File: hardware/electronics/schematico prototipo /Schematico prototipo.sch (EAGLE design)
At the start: 6 parts, among them IC1 7404N

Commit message: modifiche schematico prototipo
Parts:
- added U$6: REGOLATORE-3.3V-1A, libreria valerio:REGOLATORE-3.3V-1A
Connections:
- new net 12V: U$6.VIN
- net 3.3V: now also U$6.VOUT
- net GND: now also U$6.GND
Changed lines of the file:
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@@
 <part name="U$5" library="VHN5019" deviceset="VHN5019" device=""/>
 <part name="IC1" library="74xx-eu" library_urn="urn:adsk.eagle:library:85" deviceset="74*04" device="N" package3d_urn="urn:adsk.eagle:package:2008/1"/>
+<part name="U$6" library="libreria valerio" deviceset="REGOLATORE-3.3V-1A" device=""/>
 </parts>
 <sheets>
@@
 <instance part="IC1" gate="C" x="160.02" y="170.18"/>
 <instance part="IC1" gate="D" x="5.08" y="167.64"/>
+<instance part="U$6" gate="G$1" x="180.34" y="121.92"/>
 </instances>
 <busses>
@@
 <label x="17.78" y="76.2" size="1.27" layer="95" rot="R180" xref="yes"/>
 </segment>
+<segment>
+<pinref part="U$6" gate="G$1" pin="GND"/>
+<wire x1="180.34" y1="109.22" x2="180.34" y2="106.68" width="0.1524" layer="91"/>
+<label x="180.34" y="106.68" size="1.778" layer="95" rot="R270" xref="yes"/>
+</segment>
 </net>
 <net name="3.3V" class="0">
@@
 <label x="132.08" y="139.7" size="1.27" layer="95" xref="yes"/>
 </segment>
+<segment>
+<pinref part="U$6" gate="G$1" pin="VOUT"/>
+<wire x1="195.58" y1="119.38" x2="200.66" y2="119.38" width="0.1524" layer="91"/>
+<label x="200.66" y="119.38" size="1.778" layer="95" xref="yes"/>
+</segment>
 </net>
+<net name="12V" class="0">
+<segment>
+<pinref part="U$6" gate="G$1" pin="VIN"/>
+<wire x1="167.64" y1="119.38" x2="162.56" y2="119.38" width="0.1524" layer="91"/>
+<label x="162.56" y="119.38" size="1.778" layer="95" rot="R180" xref="yes"/>
+</segment>
+</net>

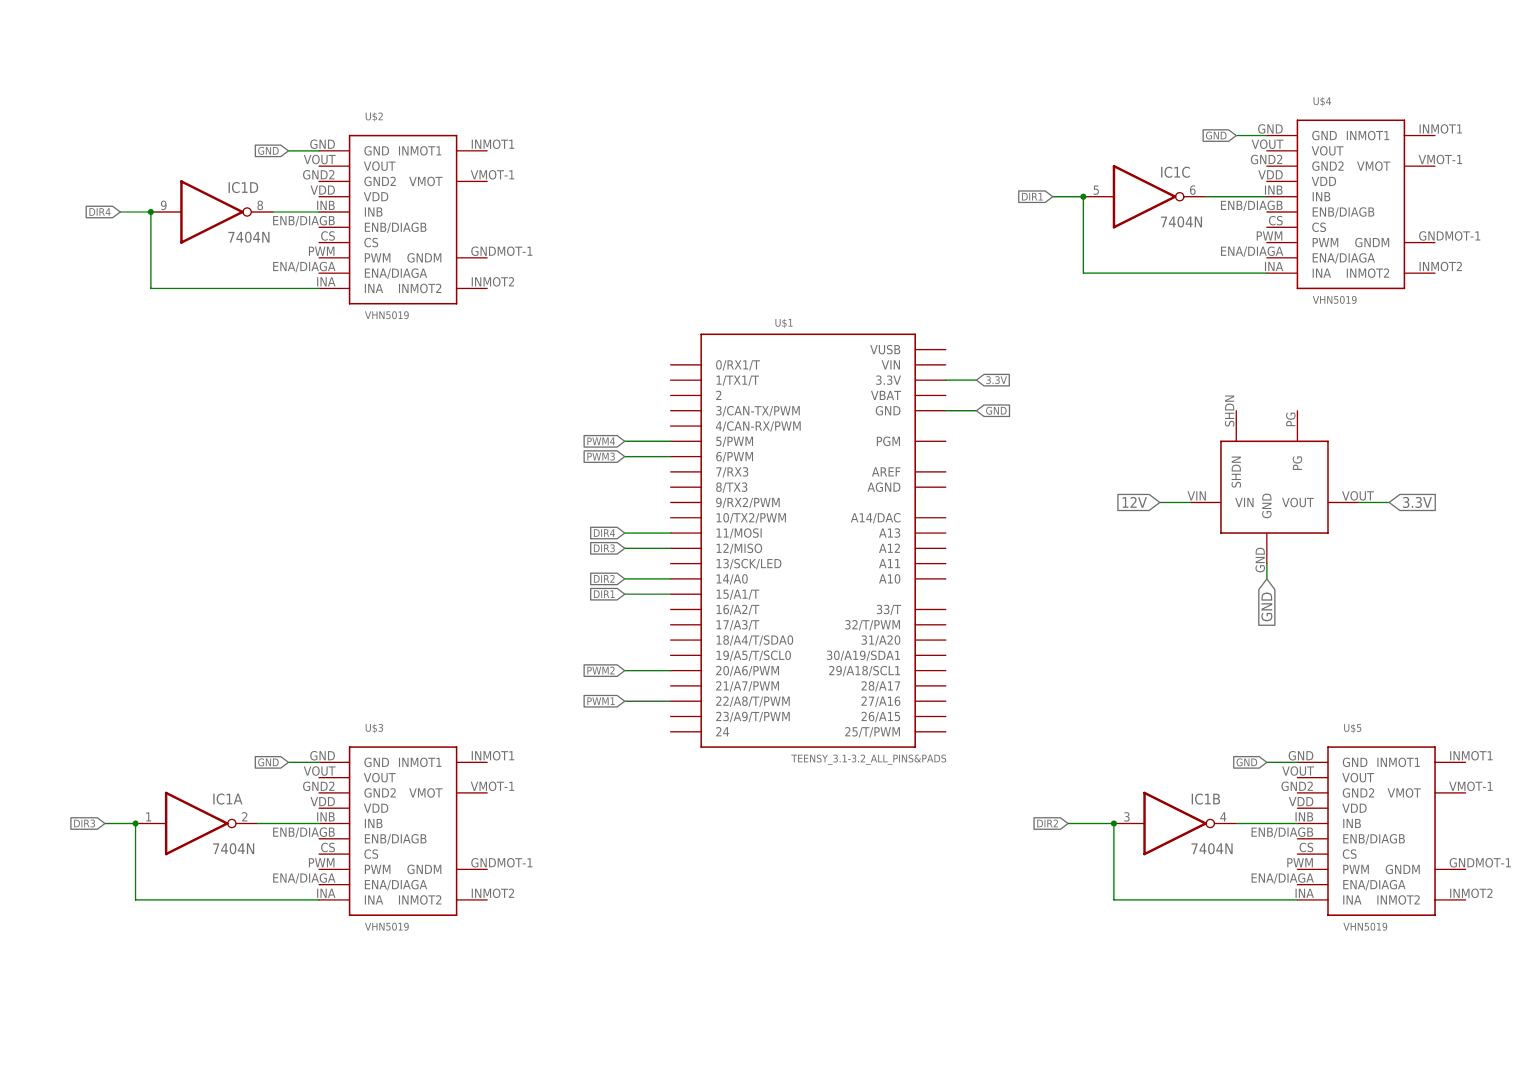
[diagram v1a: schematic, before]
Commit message: aggiunta step-down
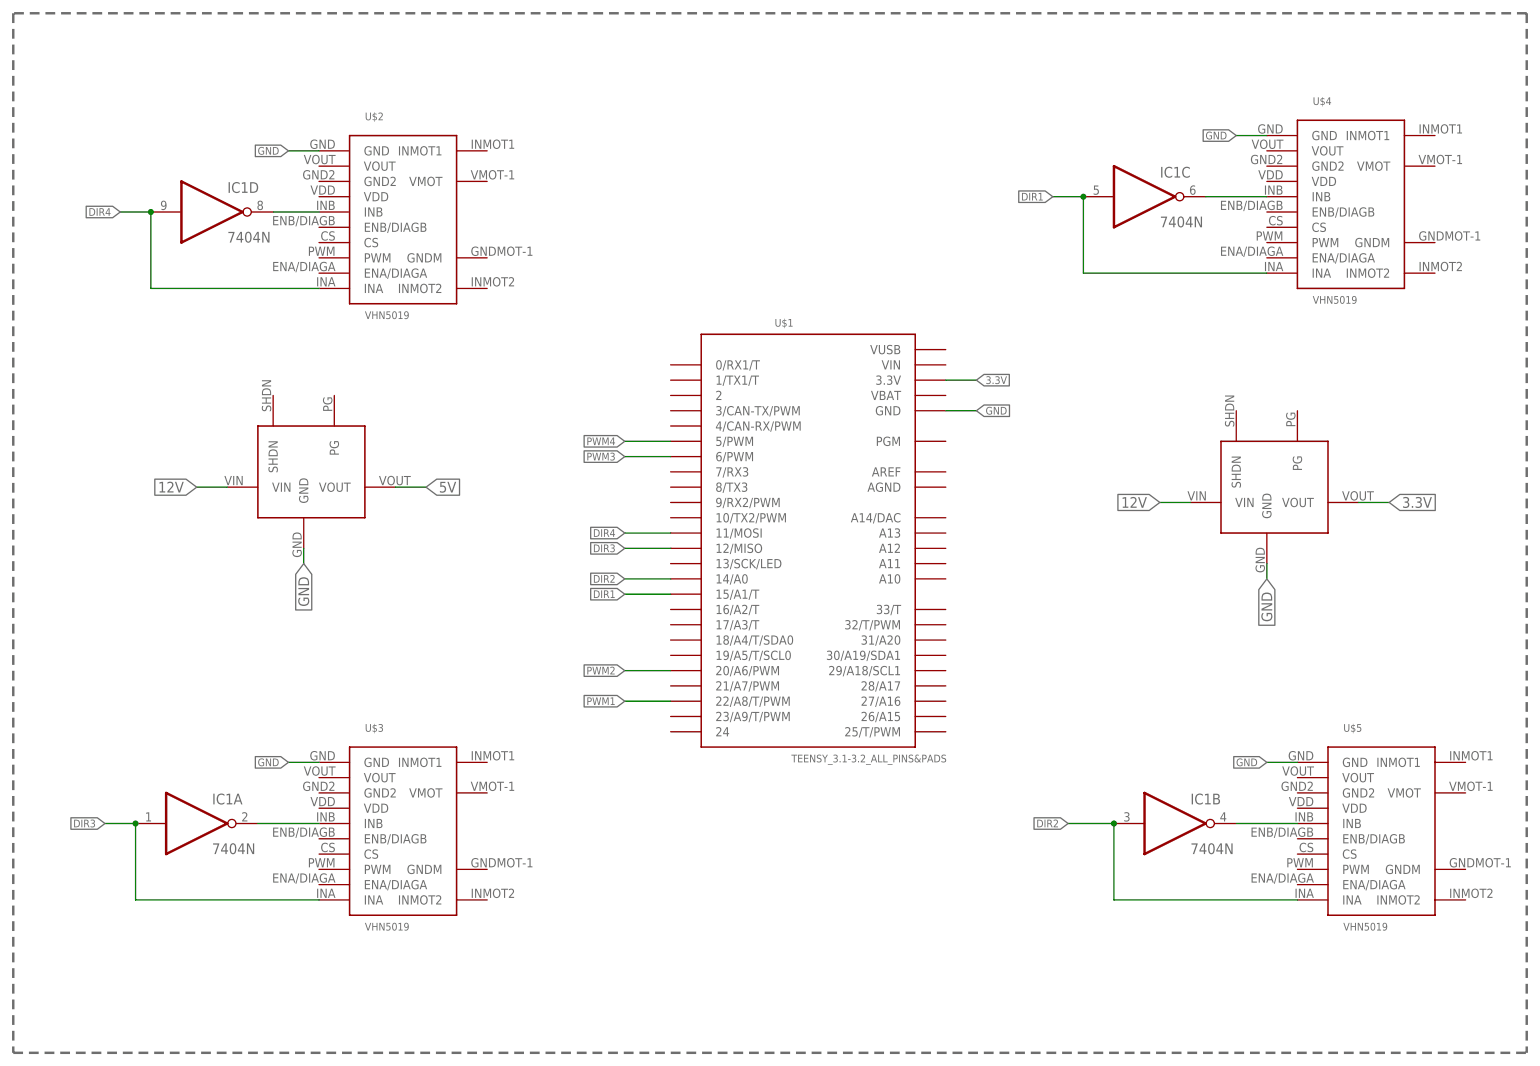
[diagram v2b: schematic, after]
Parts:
- added U$7: REGOLATORE-3.3V-1A, libreria valerio:REGOLATORE-3.3V-1A
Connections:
- new net 5V: U$7.VOUT
- net 12V: now also U$7.VIN
- net GND: now also U$7.GND
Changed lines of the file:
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@@
 <part name="IC1" library="74xx-eu" library_urn="urn:adsk.eagle:library:85" deviceset="74*04" device="N" package3d_urn="urn:adsk.eagle:package:2008/1"/>
 <part name="U$6" library="libreria valerio" deviceset="REGOLATORE-3.3V-1A" device=""/>
+<part name="U$7" library="libreria valerio" deviceset="REGOLATORE-3.3V-1A" device=""/>
 </parts>
 <sheets>
 <sheet>
 <plain>
+<wire x1="223.52" y1="200.66" x2="-27.94" y2="200.66" width="0.4064" layer="96" style="longdash"/>
+<wire x1="-27.94" y1="200.66" x2="-27.94" y2="27.94" width="0.4064" layer="96" style="longdash"/>
+<wire x1="-27.94" y1="27.94" x2="223.52" y2="27.94" width="0.4064" layer="96" style="longdash"/>
+<wire x1="223.52" y1="200.66" x2="223.52" y2="27.94" width="0.4064" layer="96" style="longdash"/>
 </plain>
 <instances>
@@
 <instance part="IC1" gate="D" x="5.08" y="167.64"/>
 <instance part="U$6" gate="G$1" x="180.34" y="121.92"/>
+<instance part="U$7" gate="G$1" x="20.32" y="124.46"/>
 </instances>
 <busses>
@@
 <label x="180.34" y="106.68" size="1.778" layer="95" rot="R270" xref="yes"/>
 </segment>
+<segment>
+<pinref part="U$7" gate="G$1" pin="GND"/>
+<wire x1="20.32" y1="111.76" x2="20.32" y2="109.22" width="0.1524" layer="91"/>
+<label x="20.32" y="109.22" size="1.778" layer="95" rot="R270" xref="yes"/>
+</segment>
 </net>
 <net name="3.3V" class="0">
@@
 <label x="162.56" y="119.38" size="1.778" layer="95" rot="R180" xref="yes"/>
 </segment>
-</net>
+<segment>
+<pinref part="U$7" gate="G$1" pin="VIN"/>
+<wire x1="7.62" y1="121.92" x2="2.54" y2="121.92" width="0.1524" layer="91"/>
+<label x="2.54" y="121.92" size="1.778" layer="95" rot="R180" xref="yes"/>
+</segment>
+</net>
+<net name="5V" class="0">
+<segment>
+<pinref part="U$7" gate="G$1" pin="VOUT"/>
+<wire x1="35.56" y1="121.92" x2="40.64" y2="121.92" width="0.1524" layer="91"/>
+<label x="40.64" y="121.92" size="1.778" layer="95" xref="yes"/>
+</segment>
+</net>
